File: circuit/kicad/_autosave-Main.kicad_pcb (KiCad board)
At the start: 2 copper layers, 110.8 x 117 mm, 104 parts, among them J1 SH3, J10 PA3, J11 SH4, J2 SH3, J3 FFC6, J4 SH6, J5 FTSH2x5, J6 FFC4, J7 SH4, J8 FFC12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

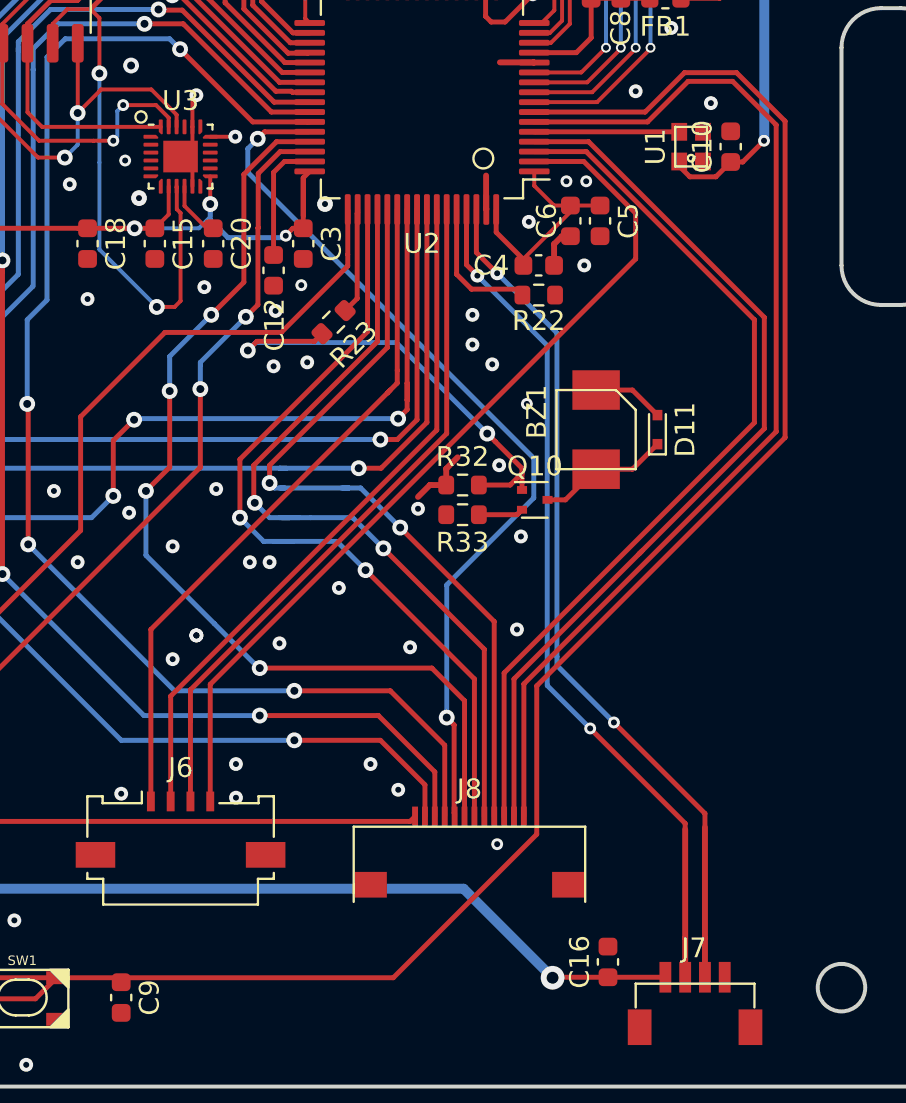
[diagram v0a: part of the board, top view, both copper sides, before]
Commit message: フットプリントの問題は解消
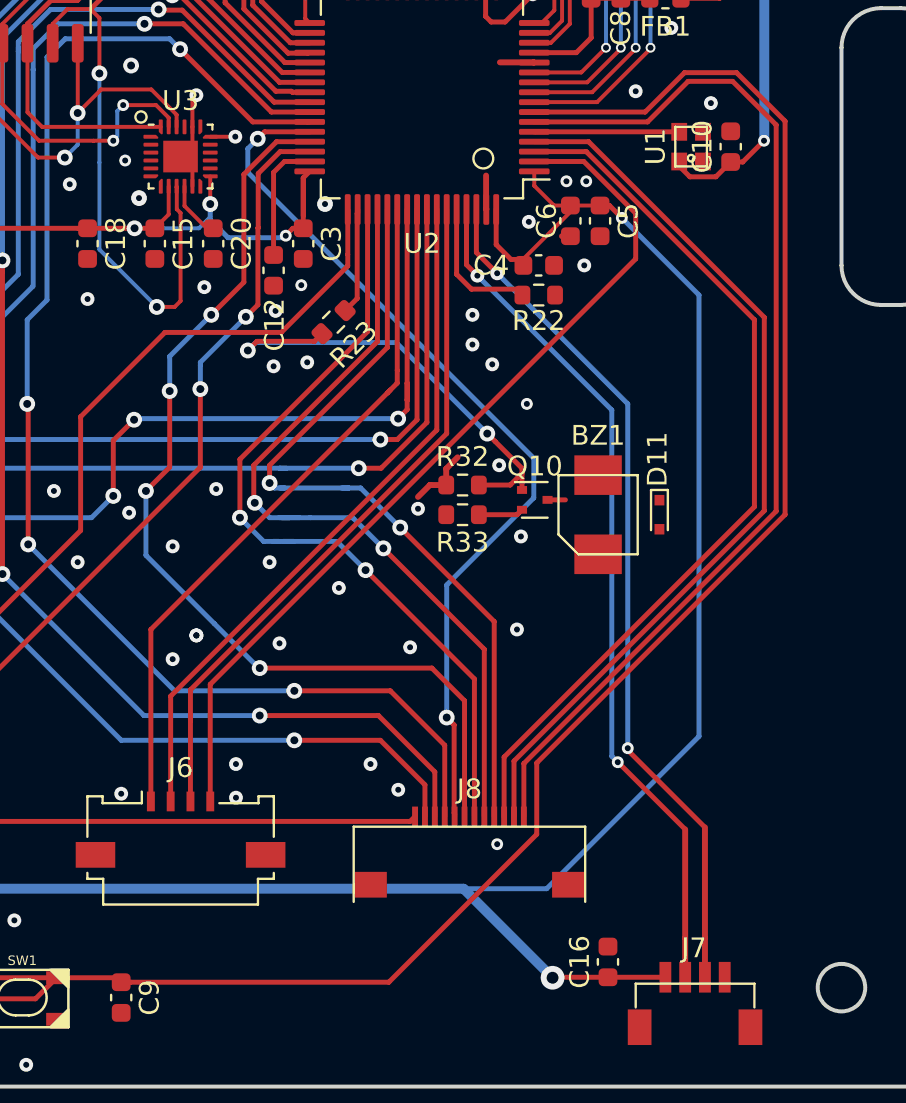
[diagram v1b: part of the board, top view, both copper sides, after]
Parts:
- moved BZ1 4.30 mm to (21.1, 18.1), turned to 270 degrees
- moved D11 4.30 mm to (24.2, 18.1), turned to 270 degrees
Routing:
- net +3V3: track 401.6 -> 442.9 mm, vias 17 -> 18
- net Net-(BZ1-Pad2): track 6.72 -> 0.90 mm
- net GND: track 35.7 -> 34.3 mm, vias 147 -> 146
